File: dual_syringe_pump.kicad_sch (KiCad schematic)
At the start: 45 parts, among them J1 USB_C_Receptacle_USB2.0_16P, Q1 SS8050, Q2 SS8050, SW1 boot, SW2 reset, U1 ESP32-WROOM-32, U2 AMS1117-3.3, U3 CH340C

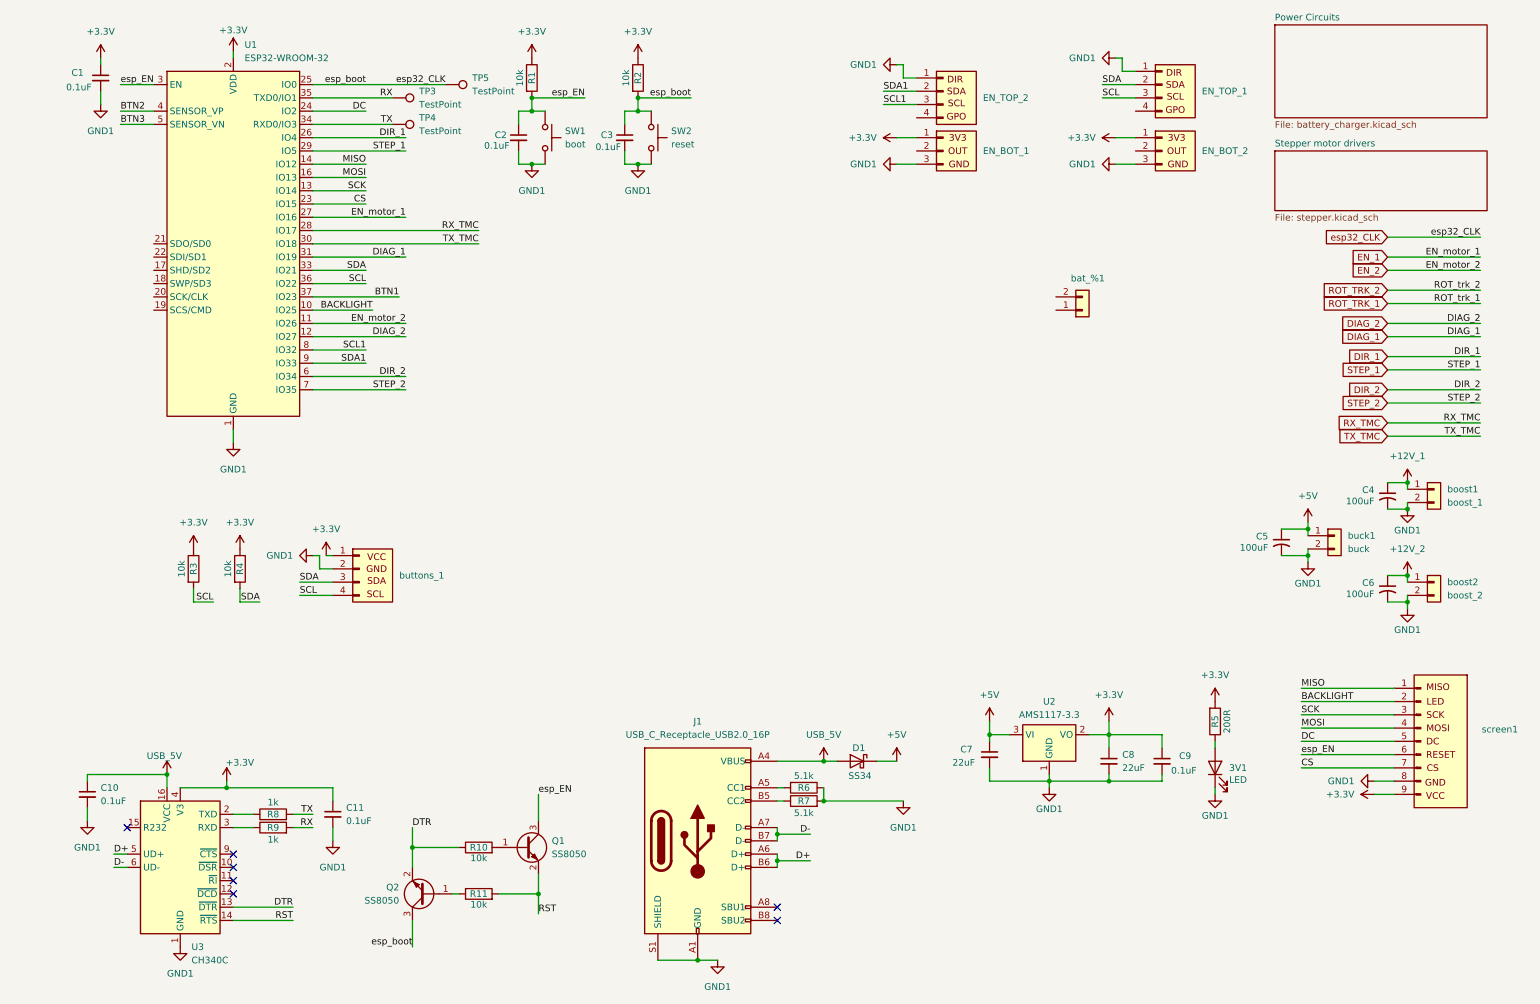
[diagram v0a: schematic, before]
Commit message: made into blocks
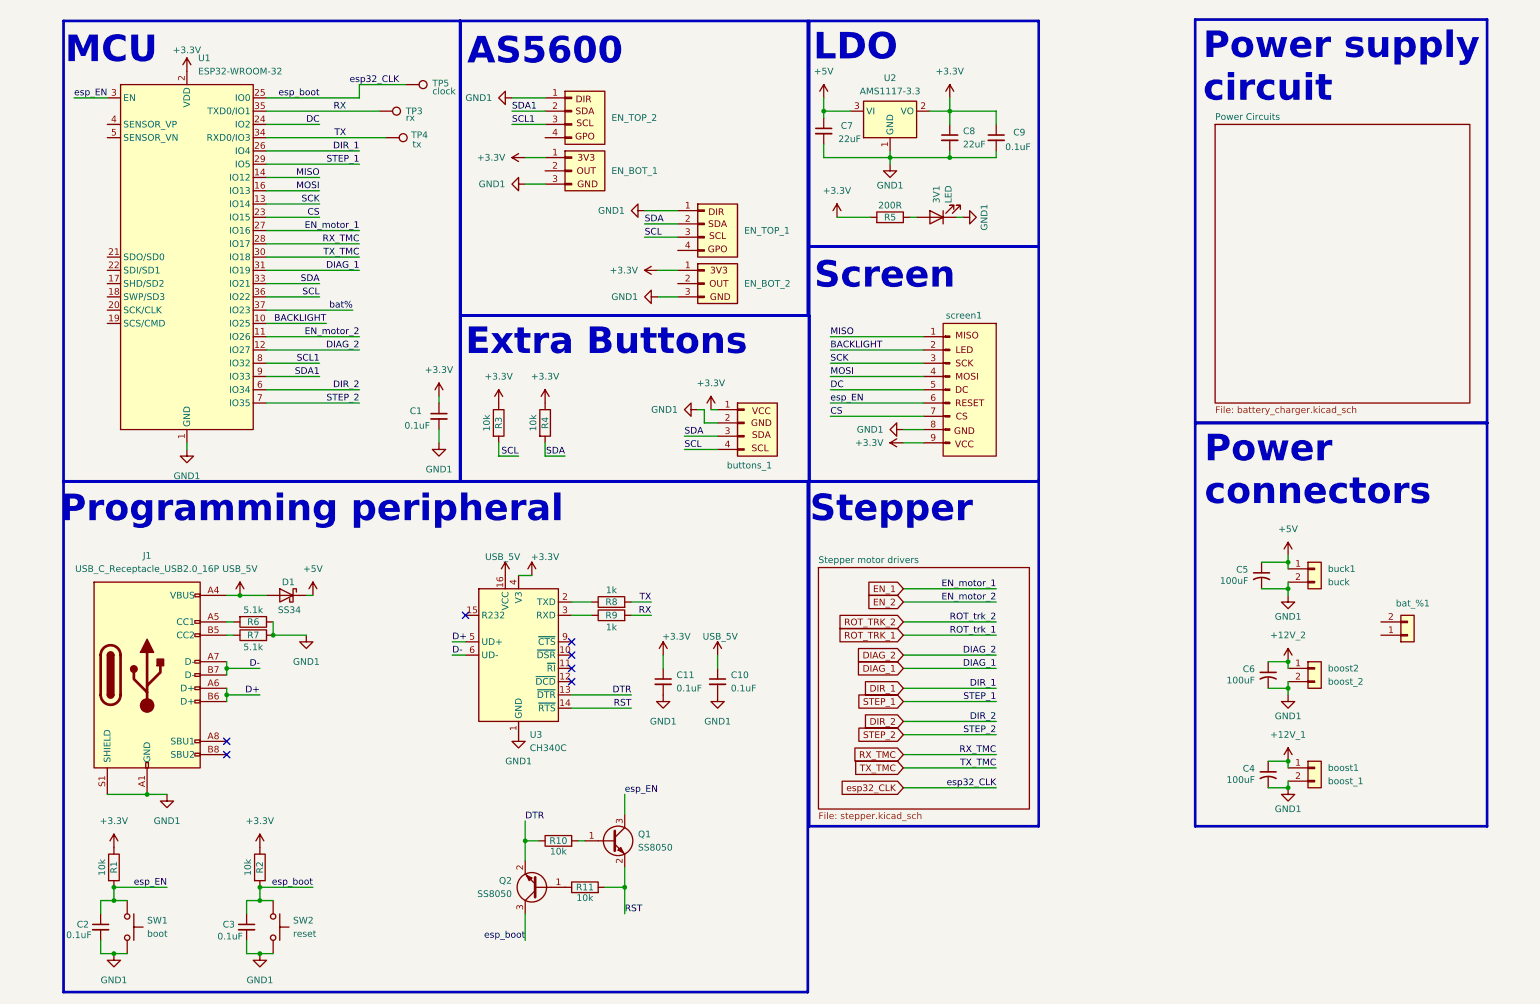
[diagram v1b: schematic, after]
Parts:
- TP3: value TestPoint -> rx
- TP4: value TestPoint -> tx
- TP5: value TestPoint -> clock
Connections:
- net BTN1 renamed bat%
- net BTN2: no longer names the net of U1.4 (SENSOR_VP)
- net BTN3: no longer names the net of U1.5 (SENSOR_VN)
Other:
- note added: "AS5600"
- note added: "Extra Buttons"
- note added: "LDO"
- note added: "MCU"
- note added: "Power connectors"
- note added: "Power supply circuit"
- note added: "Programming peripheral"
- note added: "Screen"
- note added: "Stepper"
- moved on the sheet: 3V1, C1, C10, C11, C2, C3, C4, C5, C6, C7, C8, C9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

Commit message: added power button
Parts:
- renumbered C7 to C1, C2 to C10, C3 to C11, C8 to C2, C9 to C3, C1 to C4, C11 to C7, C10 to C8, C4 to C9, EN_TOP_2 to EN_TOP_1, EN_TOP_1 to EN_TOP_2, R5 to R1, R2 to R10, R3 to R2, R4 to R3, R8 to R4, R9 to R5, R10 to R8, R1 to R9, TP5 to TP1, TP3 to TP2, TP4 to TP3, U2 to U1, U1 to U2, boost2 to boost1, boost1 to boost2
